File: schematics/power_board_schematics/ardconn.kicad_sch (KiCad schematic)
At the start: 2 parts

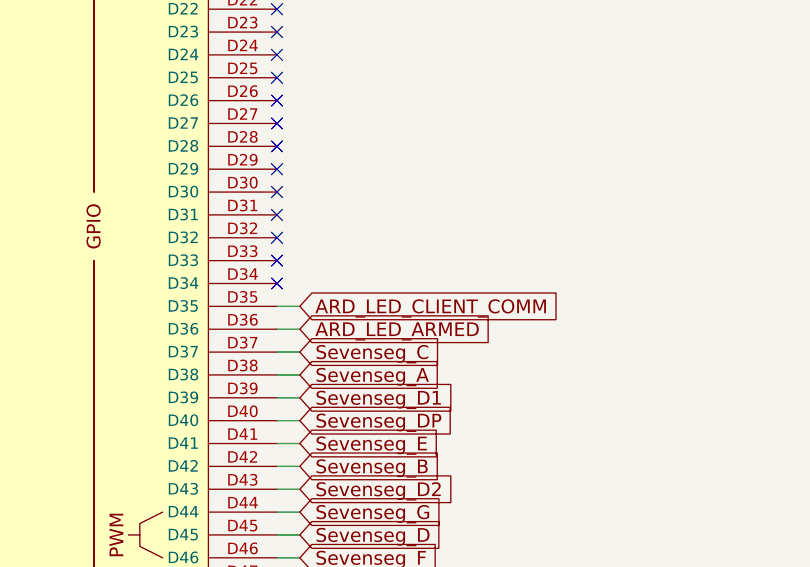
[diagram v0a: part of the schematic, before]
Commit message: Add arming switch connector to Towerside Power Board
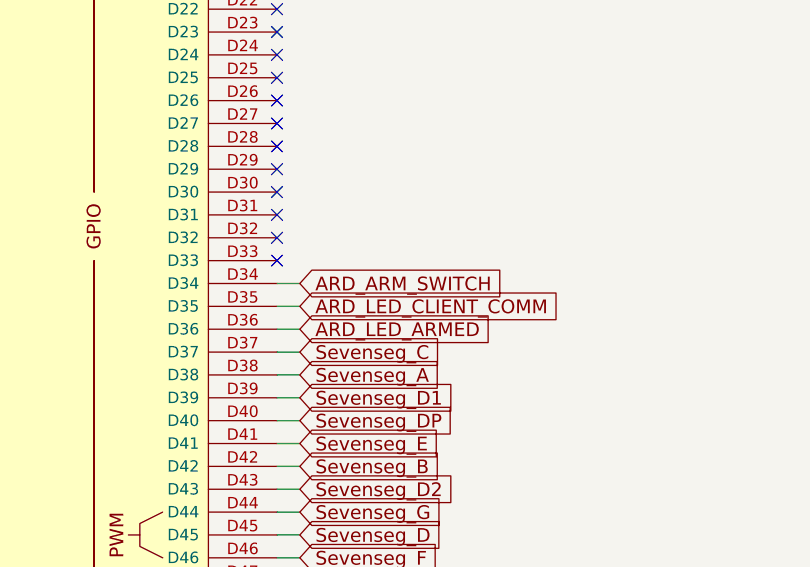
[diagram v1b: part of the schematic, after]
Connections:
- net ARD_ARM_SWITCH: now reaches XA1.D34
- no-connect marks 61 -> 60
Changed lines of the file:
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@@
   (no_connect (at 127 170.18))
   (no_connect (at 127 119.38))
-  (no_connect (at 127 121.92))
   (no_connect (at 60.96 86.36))
   (no_connect (at 60.96 78.74))
@@
     (stroke (width 0) (type default) (color 0 0 0 0))
   )
+  (wire (pts (xy 127 121.92) (xy 129.54 121.92))
+    (stroke (width 0) (type default) (color 0 0 0 0))
+  )
   (wire (pts (xy 60.96 147.32) (xy 58.42 147.32))
     (stroke (width 0) (type default) (color 0 0 0 0))
@@
     )
   )
+  (global_label "ARD_ARM_SWITCH" (shape input) (at 129.54 121.92 0) (fields_autoplaced)
+    (effects (font (size 1.524 1.524)) (justify left))
+    (property "Intersheet References" "${INTERSHEET_REFS}" (id 0) (at 151.778 121.8248 0)
+      (effects (font (size 1.524 1.524)) (justify left) hide)
+    )
+  )
